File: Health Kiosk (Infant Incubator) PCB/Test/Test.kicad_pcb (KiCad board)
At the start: 2 copper layers, 1 part

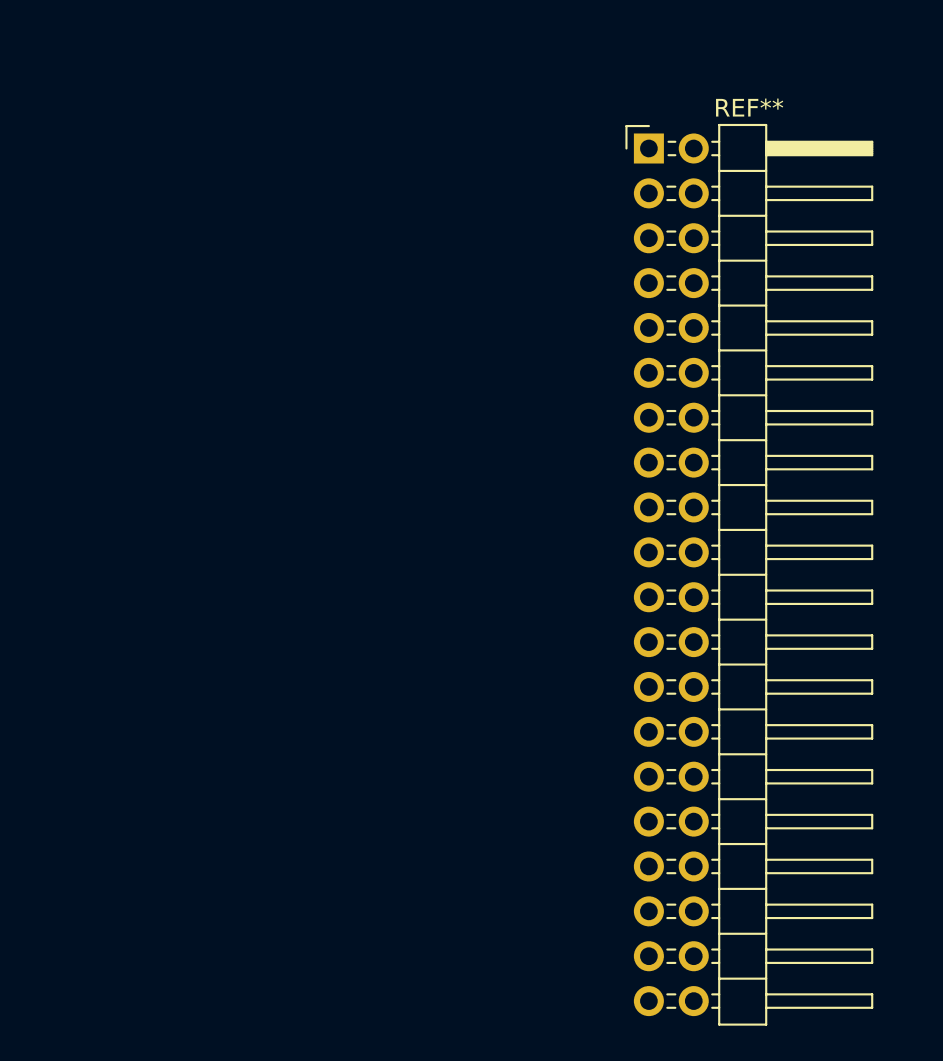
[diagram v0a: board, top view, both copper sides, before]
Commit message: PCB Design Finished (Buck footprint left)
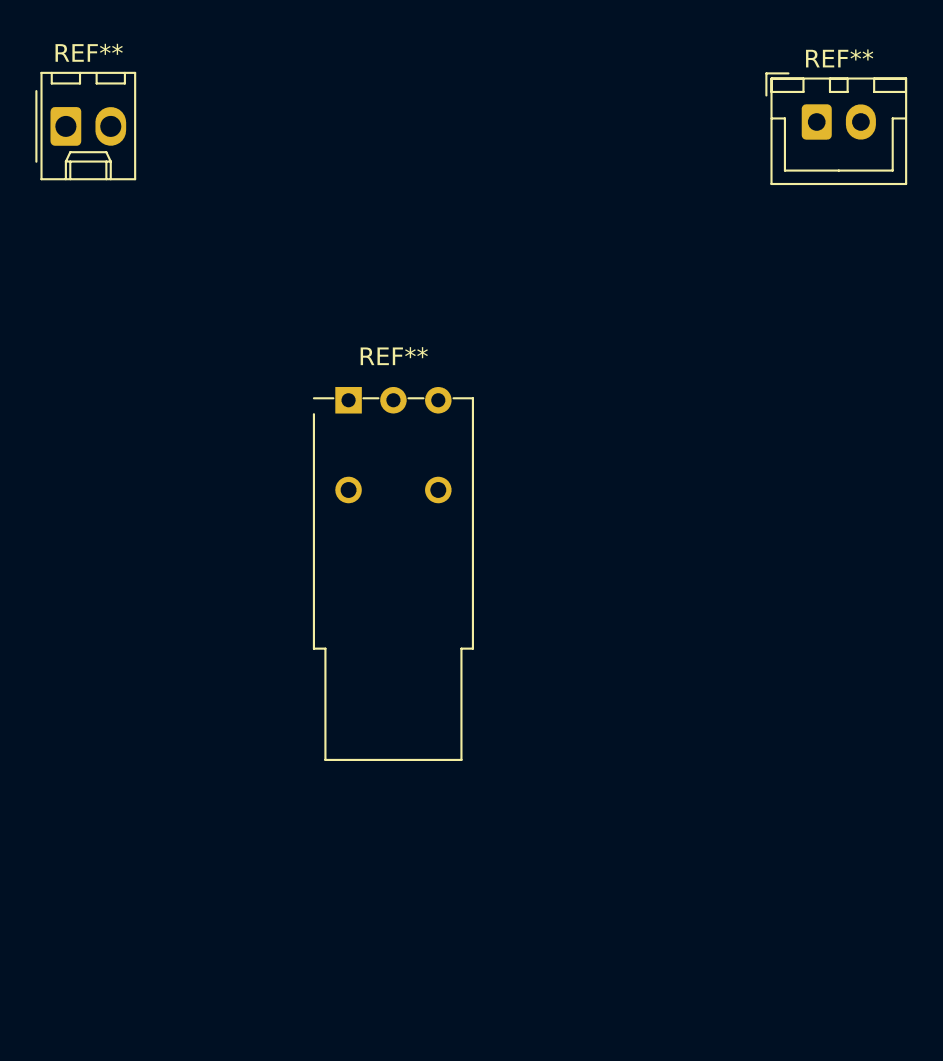
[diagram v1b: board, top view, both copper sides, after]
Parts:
- removed the REF** at (150.5, 82.5)
- added REF**: SW_NKK_BB15AH, Button_Switch_THT:SW_NKK_BB15AH, F.Cu at (133.5, 96.8)
- added REF**: JST_XH_B2B-XH-A_1x02_P2.50mm_Vertical, Connector_JST:JST_XH_B2B-XH-A_1x02_P2.50mm_Vertical, F.Cu at (160.0, 81.0)
- added REF**: Molex_KK-254_AE-6410-02A_1x02_P2.54mm_Vertical, Connector_Molex:Molex_KK-254_AE-6410-02A_1x02_P2.54mm_Vertical, F.Cu at (117.5, 81.2)
